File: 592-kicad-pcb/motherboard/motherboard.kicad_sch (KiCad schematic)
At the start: 10 parts, among them U10 NUCLEO144-F746ZG, U7 STM32H563ZITx

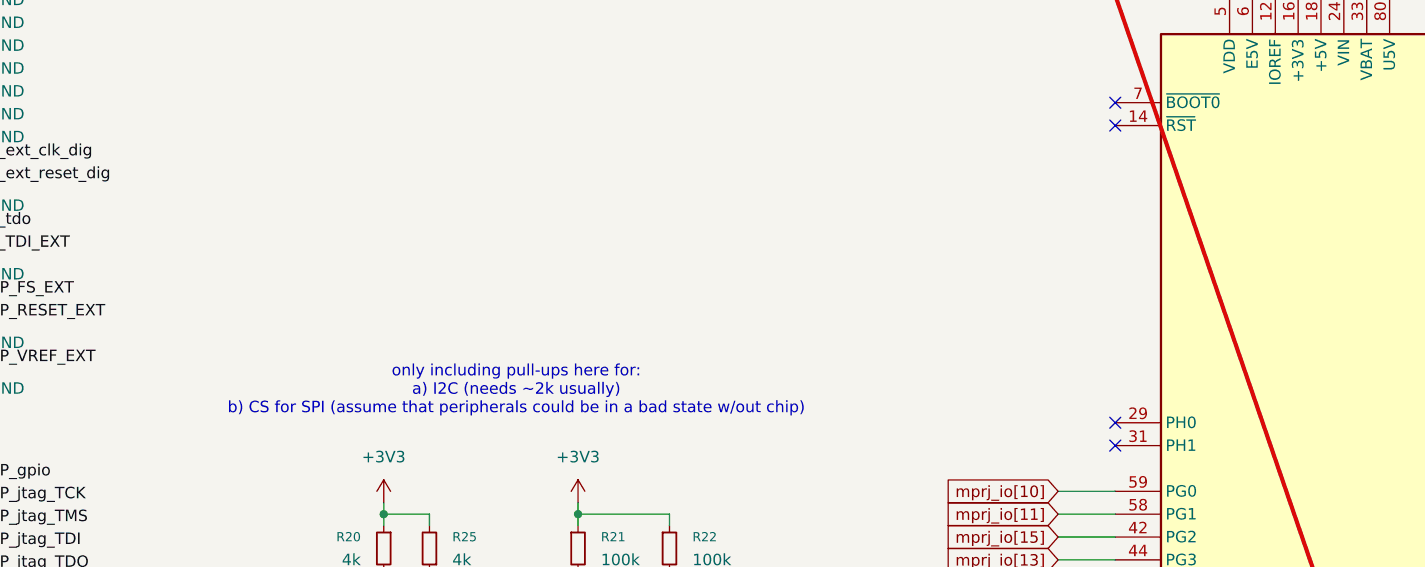
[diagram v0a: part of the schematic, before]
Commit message: add jlc stackup, size pulldowns
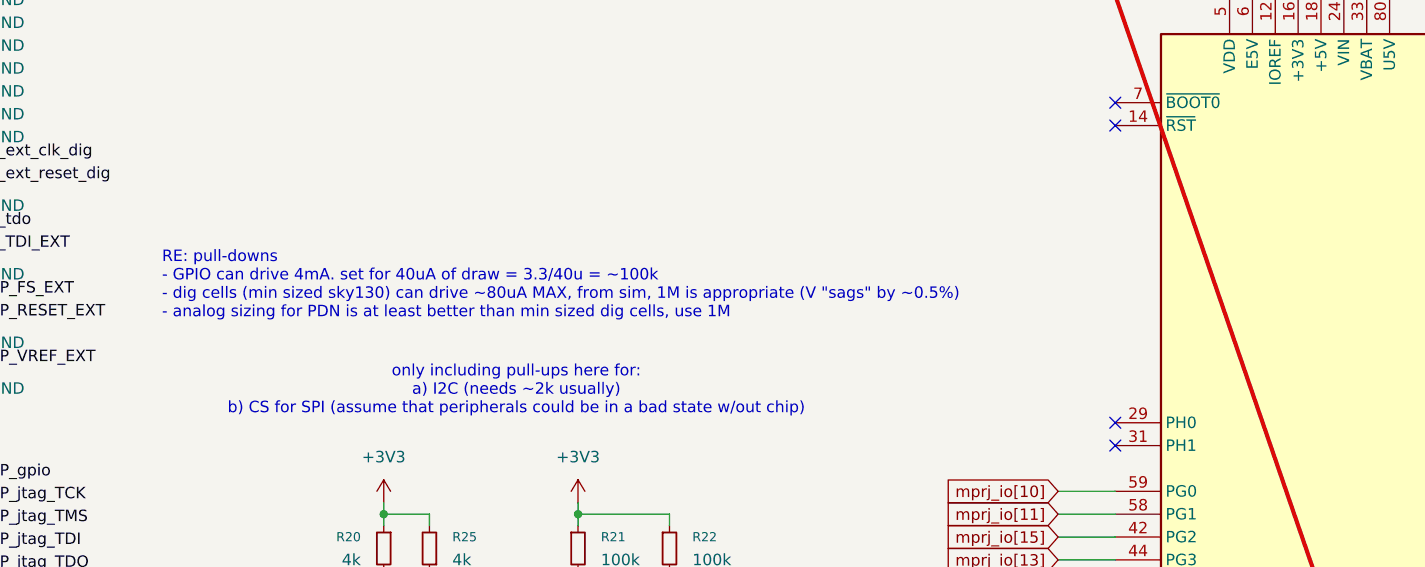
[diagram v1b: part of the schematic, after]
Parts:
- R12, R13, R20, R21, R22, R25: footprint (none) -> Resistor_SMD:R_0603_1608Metric
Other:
- note added: "RE: pull-downs - GPIO can drive 4mA. set for 40uA of draw = 3.3/40u = ~100k - dig cells (min sized sky130) can drive ~80uA MAX, from sim, 1M is appropriate (V "sags" by ~0.5%) - analog sizing for PDN is at least better than min sized dig cells, use 1M"

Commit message: rough layout stufF
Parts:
- U7: footprint Package_QFP:LQFP-144_20x20mm_P0.5mm -> (none)

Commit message: Added most of nucleo domain to the motherboard schematic
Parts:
- added C12: 10uF, symbol Device:C
- added C13: 0.1uF, symbol Device:C
- added C14: 0.01uf - CC0805JRX7R9BB103, Capacitor_SMD:C_0805_2012Metric, symbol Device:C
- added C15, C16, C17, C18, C19, C20, C21, C22, C23, C4: 0.1uf - CC0805KRX7R9BB104, Capacitor_SMD:C_0805_2012Metric, symbol Device:C
- added D1, D2: LED - 17-215SURC/S530-A2/TR8, LED_SMD:LED_1206_3216Metric, symbol Device:LED
- added J10: Conn_01x02_Male, Connector_PinHeader_2.54mm:PinHeader_1x02_P2.54mm_Vertical, symbol Connector:Conn_01x02_Male
- added J11: Conn_01x02_Female, Connector_PinHeader_2.54mm:PinHeader_1x02_P2.54mm_Vertical, symbol Connector:Conn_01x02_Female
- added R30, R37, R38, R39, R40, R41, R42, R43, R44, R45, R46, R47, R48: 10k - RC0805FR-0710KL, Resistor_SMD:R_0805_2012Metric, symbol Device:R
- added R31: 12K 1% - 0805W8F1202T5E, Resistor_SMD:R_0805_2012Metric, symbol Device:R
- added R33, R34: 150 - 0805W8J0151T5E, Resistor_SMD:R_0805_2012Metric, symbol Device:R
- added R35, R36: 10k, Resistor_SMD:R_0805_2012Metric, symbol Device:R
- added U11: SD Card Holder, symbol New_Library:sd_card_connector
- added U12: ~, symbol New_Library:usb_C_Connector
- added U13: FT232H, Package_DFN_QFN:QFN-48-1EP_8x8mm_P0.5mm_EP6.2x6.2mm, symbol Interface_USB:FT232H
- added U14, U15: SN74LVC1G125DCKR, SOT65P210X110-5N, symbol Caravel_board:SN74LVC1G125DCKR
- added U16, U17: W25Q32JVZP, strive_foot_prints:SOIC127P790X216-8N, symbol Caravel_board:W25Q32FVSS
- added X1: DSC6001_10MHZ, strive_foot_prints:DSC6001JE1A-010.0000, symbol Oscillator:XO91
- added Y3: CSTNE12M0GH5L000R0, strive_foot_prints:CSTNE12M0GH5L000R0, symbol Device:Crystal_GND2
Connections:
- net MCU_SDA is gone; now on net I2C1_SDA: R13.1, U10.77 (PB9)
- net +3V3: now also C4.2, X1.4 (V+)
- net CHIP_spi_flash_0_cs_0: now also R37.1, U11.2 (CD/DAT3), U16.1 (~{CS})
- net CHIP_spi_flash_0_dq_0: now also R40.1, U11.3 (CMD), U16.5 (SI(D0))
- net CHIP_spi_flash_0_dq_1: now also R38.1, U11. (CLK), U16.2 (SO(D1))
- net CHIP_spi_flash_0_dq_2: now also R39.1, U16.3 (~{WP}(D2))
- net CHIP_spi_flash_0_dq_3: now also R42.1, U16.7 (~{HOLD}(D3))
- net CHIP_spi_flash_0_sck: now also R41.1, U11. (CLK), U16.6 (SCK)
- net GND: now also C12.2, C13.2, C14.1, C15.1, C16.1, C17.1, C18.1, C19.1, C20.1, C21.1, C22.2, C23.2, C4.1, J10.2 (Pin_2), J11.1 (Pin_1), R31.1, U11. (CLK), U12.A1 (GND), U12.A12 (GND), U12.B1 (GND), U12.B12 (GND), U13.10 (GND), U13.11 (GND), U13.22 (GND), U13.23 (GND), U13.35 (GND), U13.36 (GND), U13.4 (AGND), U13.41 (AGND), U13.42 (TEST), U13.47 (GND), U13.48 (GND), U13.9 (AGND), U14.3 (GND), U15.3 (GND), U16.4 (GND), U17.4 (GND), X1.2 (GND), Y3.2
- net ~{MR}: now also U13.25 (ACBUS1)
- net I2C2_SDA: now reaches U7.10 (PF0)
- net I2C2_SCL: now reaches U7.11 (PF1)
- net SPI1_MISO: now reaches U7.124 (PG9)
- net I2C1_SCL: now reaches U7.136 (PB6)
- net I2C1_SDA: now reaches U7.137 (PB7)
- net I3C1_SCL: now reaches U7.15 (PF5)
- net SPI2_MOSI: now reaches U7.27 (PC1)
- net SPI2_MISO: now reaches U7.28 (PC2)
- net UART4_TX: now reaches U7.34 (PA0)
- net ADC1_INP1: now reaches U7.35 (PA1)
- net SPI1_SCK: now reaches U7.41 (PA5)
- net ADC1_INP3: now reaches U7.42 (PA6)
- net SPI1_MOSI: now reaches U7.43 (PA7)
- net ADC2_INP4: now reaches U7.44 (PC4)
- net ADC2_INP2: now reaches U7.53 (PF13)
- net I3C1_SDA: now reaches U7.55 (PF15)
- net SPI2_SCK: now reaches U7.69 (PB10)
- net UART5_RX: now reaches U7.73 (PB12)
- net UART5_RX: now also U7.74 (PB13)
- net UART4_RX: now reaches U7.80 (PD11)
- new net: U13.1 (XCSI), Y3.1
- new net: U13.2 (XCSO), Y3.3
- new net: D2.1 (K), U13.26 (ACBUS2)
- new net: D1.1 (K), U13.27 (ACBUS3)
- new net: C14.2, R30.1, U13.34 (~{RESET})
- new net: C16.2, U13.37 (VCCA)
- new net: C15.2, U13.38 (VCCCORE)
- new net: R31.2, U13.5 (REF)
- new net: D1.2 (A), R33.1
- new net: J10.1 (Pin_1), X1.1 (EN)
- new net: D2.2 (A), R34.1
- new net +3.3V: C12.1, C13.1, C22.1, C23.1, R35.1, R36.1, R37.2, R38.2, R39.2, R40.2, R41.2, R42.2, R43.2, R44.2, R45.2, R46.2, R47.2, R48.2, U11.4 (VDD), U14.5 (VCC), U15.5 (VCC), U16.8 (VCC), U17.8 (VCC)
- new net EN_V1.8: U13.29 (ACBUS5)
- new net EN_V3.3: U13.30 (ACBUS6)
- new net FTDI_D+: U12.A6 (D+), U12.B6 (D+), U13.7 (DP)
- new net FTDI_D-: U12.A7 (D-), U12.B7 (D-), U13.6 (DM)
- new net FTDI_V3.3: C17.2, C18.2, C19.2, C20.2, C21.2, R30.2, R33.2, R34.2, U13.12 (VCCIO), U13.24 (VCCIO), U13.3 (VPHY), U13.39 (VCCD), U13.40 (VREGIN), U13.46 (VCCIO), U13.8 (VPLL)
- new net MEM_CS: R43.1, U17.1 (~{CS})
- new net MEM_SCK: R47.1, U17.6 (SCK)
- new net MEM_SI: R46.1, U17.5 (SI(D0))
- new net MEM_SO: R44.1, U17.2 (SO(D1))
- new net USB_CS1: U13.16 (ADBUS3)
- new net USB_SCK_TXD: U13.13 (ADBUS0), U14.2 (A)
- new net USB_SI: U13.15 (ADBUS2)
- new net USB_SO_RXD: U13.14 (ADBUS1), U15.4 (Y)
- new net mprj_io[5]_ser_rx: U14.4 (Y)
- new net mprj_io[6]_ser_tx: U15.2 (A)
- new net xclk: X1.3 (OUT)
- new net ~{MEM_HOLD}: R48.1, U17.7 (~{HOLD}(D3))
- new net ~{MEM_WP}: R45.1, U17.3 (~{WP}(D2))
- new net ~{UART_EN}: J11.2 (Pin_2), R35.2, R36.2, U13.21 (ACBUS0), U14.1 (~{OE}), U15.1 (~{OE})
- no-connect marks 39 -> 49
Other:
- note added: "Buffers to enable FTDI UART interface"
- note added: "Caravel 10MHz Clock Source"
- note added: "FTDI Module"
- note added: "Flash memory interface with Caravel"
- note added: "Flash memory interface with Rocket Chip (IF SD CARD WILL NOT WORK)"
- note added: "NOTE: Leave DAT2 and DAT1 unconnected as they are not used in SPI Mode"
- note added: "SD Memory Card Holder (ONLY USE IF FOUND TO BE WORKING)"
- note added: "TODO: Maybe add 10kOhm pull up resistors to CMD, DAT0, and CD/DAT3"
- note added: "TODO: Potentially connect to clock module?"
- note added: "TODO: check the configuration for dq_2 and dq_3 to determine whether the signals need to be inverted"
- note added: "USB_C_Connector_FTDI"
- moved on the sheet: R12, R13, U10

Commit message: resaved maybe more updates on the motherboard schematic
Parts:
- removed C23: 0.1uf - CC0805KRX7R9BB104, Capacitor_SMD:C_0805_2012Metric, symbol Device:C
- removed R43, R44, R45, R46, R47, R48: 10k - RC0805FR-0710KL, Resistor_SMD:R_0805_2012Metric, symbol Device:R
- removed U17: W25Q32JVZP, strive_foot_prints:SOIC127P790X216-8N, symbol Caravel_board:W25Q32FVSS
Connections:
- net SPI1_SCK: now also U7.126 (PG11); no longer U7.41 (PA5)
- net GPIO_Output: now reaches U7.114 (PD0)
- net GPIO_Output: now also U7.115 (PD1), U7.116 (PD2)
- net DAC1_OUT1: now reaches U7.40 (PA4)
- new net DAC1_OUT2: U7.41 (PA5)
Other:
- note added: "Not sure what this does/what it needs to connect to on the Nucleo"
- note added: "TODO: Find out what the hell this connects to"
- note removed: "Flash memory interface with Caravel"
- note removed: "TODO: Potentially connect to clock module?"
- moved on the sheet: U7

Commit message: Added the irq and irq2 inputs to the nucleo
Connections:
- net GPIO_Output is gone; now on net CHIP_i2c_0_scl (irq2 on Caravan): U7.114 (PD0), U7.115 (PD1), U7.116 (PD2)
- net xclk is gone; now on net CHIP_clk: X1.3 (OUT)
- net MCU_TIM_NFCCLK: now also U7.60 (PE9)
- net CHIP_i2c_0_scl (irq2 on Caravan): now reaches U7.117 (PD3)
- net CHIP_i2c_0_scl (irq2 on Caravan): now also U7.118 (PD4)
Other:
- note removed: "Not sure what this does/what it needs to connect to on the Nucleo"
- note removed: "TODO: Find out what the hell this connects to"

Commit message: Added the rest of the ports
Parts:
- C15, C16, C17, C18, C19, C20, C21, C22, C4: value 0.1uf - CC0805KRX7R9BB104 -> 0.1uf
- R33, R34: value 150 - 0805W8J0151T5E -> 150
- R37, R38, R39, R40, R41, R42: value 10k - RC0805FR-0710KL -> 10k
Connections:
- net ~{MR}: no longer U13.25 (ACBUS1)
- net EN_V1.8: no longer names the net of U13.29 (ACBUS5)
- net EN_V3.3: no longer names the net of U13.30 (ACBUS6)
- net FTDI_V3.3 renamed 3V3
- net mprj_io[5]_ser_rx renamed CHIP_spi_0_dq_0 (ser_rx on Caravan)
- net mprj_io[6]_ser_tx renamed CHIP_spi_0_cs_0 (ser_tx on Caravan)

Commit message: clean up schematics, add proper connectors
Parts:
- removed C12: 10uF, symbol Device:C
- removed C13: 0.1uF, symbol Device:C
- removed C14: 0.01uf - CC0805JRX7R9BB103, Capacitor_SMD:C_0805_2012Metric, symbol Device:C
- removed C15, C16, C17, C18, C19, C20, C21, C22, C4: 0.1uf, Capacitor_SMD:C_0805_2012Metric, symbol Device:C
- removed CON1, CON2: ~, TinyTapeout:FH-00148_PinSocket_2x20_P2.54mm, symbol Connector_Generic:Conn_02x20_Odd_Even
- removed D1, D2: LED - 17-215SURC/S530-A2/TR8, LED_SMD:LED_1206_3216Metric, symbol Device:LED
- removed J10: Conn_01x02_Male, Connector_PinHeader_2.54mm:PinHeader_1x02_P2.54mm_Vertical, symbol Connector:Conn_01x02_Male
- removed J11: Conn_01x02_Female, Connector_PinHeader_2.54mm:PinHeader_1x02_P2.54mm_Vertical, symbol Connector:Conn_01x02_Female
- removed R12, R13, R20, R25: 4k, Resistor_SMD:R_0603_1608Metric, symbol Device:R_Small
- removed R21, R22: 100k, Resistor_SMD:R_0603_1608Metric, symbol Device:R_Small
- removed R30: 10k - RC0805FR-0710KL, Resistor_SMD:R_0805_2012Metric, symbol Device:R
- removed R31: 12K 1% - 0805W8F1202T5E, Resistor_SMD:R_0805_2012Metric, symbol Device:R
- removed R33, R34: 150, Resistor_SMD:R_0805_2012Metric, symbol Device:R
- removed R35, R36, R37, R38, R39, R40, R41, R42: 10k, Resistor_SMD:R_0805_2012Metric, symbol Device:R
- removed U10: NUCLEO144-F746ZG, Module:ST_Morpho_Connector_144_STLink, symbol MCU_Module:NUCLEO144-F746ZG
- removed U11: SD Card Holder, symbol New_Library:sd_card_connector
- removed U12: ~, symbol New_Library:usb_C_Connector
- removed U13: FT232H, Package_DFN_QFN:QFN-48-1EP_8x8mm_P0.5mm_EP6.2x6.2mm, symbol Interface_USB:FT232H
- removed U14, U15: SN74LVC1G125DCKR, SOT65P210X110-5N, symbol Caravel_board:SN74LVC1G125DCKR
- removed U16: W25Q32JVZP, strive_foot_prints:SOIC127P790X216-8N, symbol Caravel_board:W25Q32FVSS
- removed X1: DSC6001_10MHZ, strive_foot_prints:DSC6001JE1A-010.0000, symbol Oscillator:XO91
- removed Y3: CSTNE12M0GH5L000R0, strive_foot_prints:CSTNE12M0GH5L000R0, symbol Device:Crystal_GND2
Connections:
- removed net CHIP_i2c_0_scl (irq2 on Caravan): U7.114 (PD0), U7.115 (PD1), U7.116 (PD2), U7.117 (PD3), U7.118 (PD4)
- net DAC1_OUT1 renamed MCU_DAC_VREF
- net I2C1_SCL renamed MCU_SCK
- net I2C1_SDA renamed MCU_SDA
- new net CHIP_i2c_0_scl_(irq2_on_Caravan): U7.118 (PD4)
- new net CHIP_spi_0_sck_(irq_on_Caravan): U7.117 (PD3)
- new net MCU_GPIO_FS_SEL: U7.116 (PD2)
- new net MCU_GPIO_NFCCLK_SEL: U7.115 (PD1)
- new net MCU_GPIO_RESET_AFE: U7.114 (PD0)
- no-connect marks 49 -> 0
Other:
- added sheet chip_connection (chip_connection.kicad_sch)
- added sheet ftdi (ftdi.kicad_sch)
- added sheet memory (memory.kicad_sch)
- sheet clock_sources ports: added CARAVEL_CLK_10M, CARAVEL_CLK_SEL; removed none
- note added: "DAC1_OUT1"
- note added: "GPIO_Output (all on this bank)"
- note added: "I2C1_SCL"
- note added: "I2C1_SDA"
- note added: "MASTER TODO: 1) verify caravel support chip configuration 2) correct pull up/down resistors 3) update to new FTDI chip 4) add voltage regulators 5) update nucleo symbol, assign/document pins 6) verify memory interface pinsouts for rocketchip, add connector 7) make connector pinouts match PMOD/JTAG interface on arty"
- note added: "TIM1_CH1"
- note removed: "Buffers to enable FTDI UART interface"
- note removed: "Caravel 10MHz Clock Source"
- note removed: "FTDI Module"
- note removed: "Flash memory interface with Rocket Chip (IF SD CARD WILL NOT WORK)"
- note removed: "NOTE: Leave DAT2 and DAT1 unconnected as they are not used in SPI Mode"
- note removed: "RE: pull-downs - GPIO can drive 4mA. set for 40uA of draw = 3.3/40u = ~100k - dig cells (min sized sky130) can drive ~80uA MAX, from sim, 1M is appropriate (V "sags" by ~0.5%) - analog sizing for PDN is at least better than min sized dig cells, use 1M"
- note removed: "SD Memory Card Holder (ONLY USE IF FOUND TO BE WORKING)"
- note removed: "TODO: Maybe add 10kOhm pull up resistors to CMD, DAT0, and CD/DAT3"
- note removed: "TODO: check the configuration for dq_2 and dq_3 to determine whether the signals need to be inverted"
- note removed: "TODO: use new zio connector pinout?"
- note removed: "USB_C_Connector_FTDI"
- note removed: "add pull-downs where applicable for inputs to chips from the NFC chip consider just using GPIO PDN on STM. need to add discretes for other chips"
- note removed: "connectors for daughterboard (TODO keep up to date when finalized)"
- note removed: "only including pull-ups here for: a) I2C (needs ~2k usually) b) CS for SPI (assume that peripherals could be in a bad state w/out chip)"
- moved on the sheet: U7

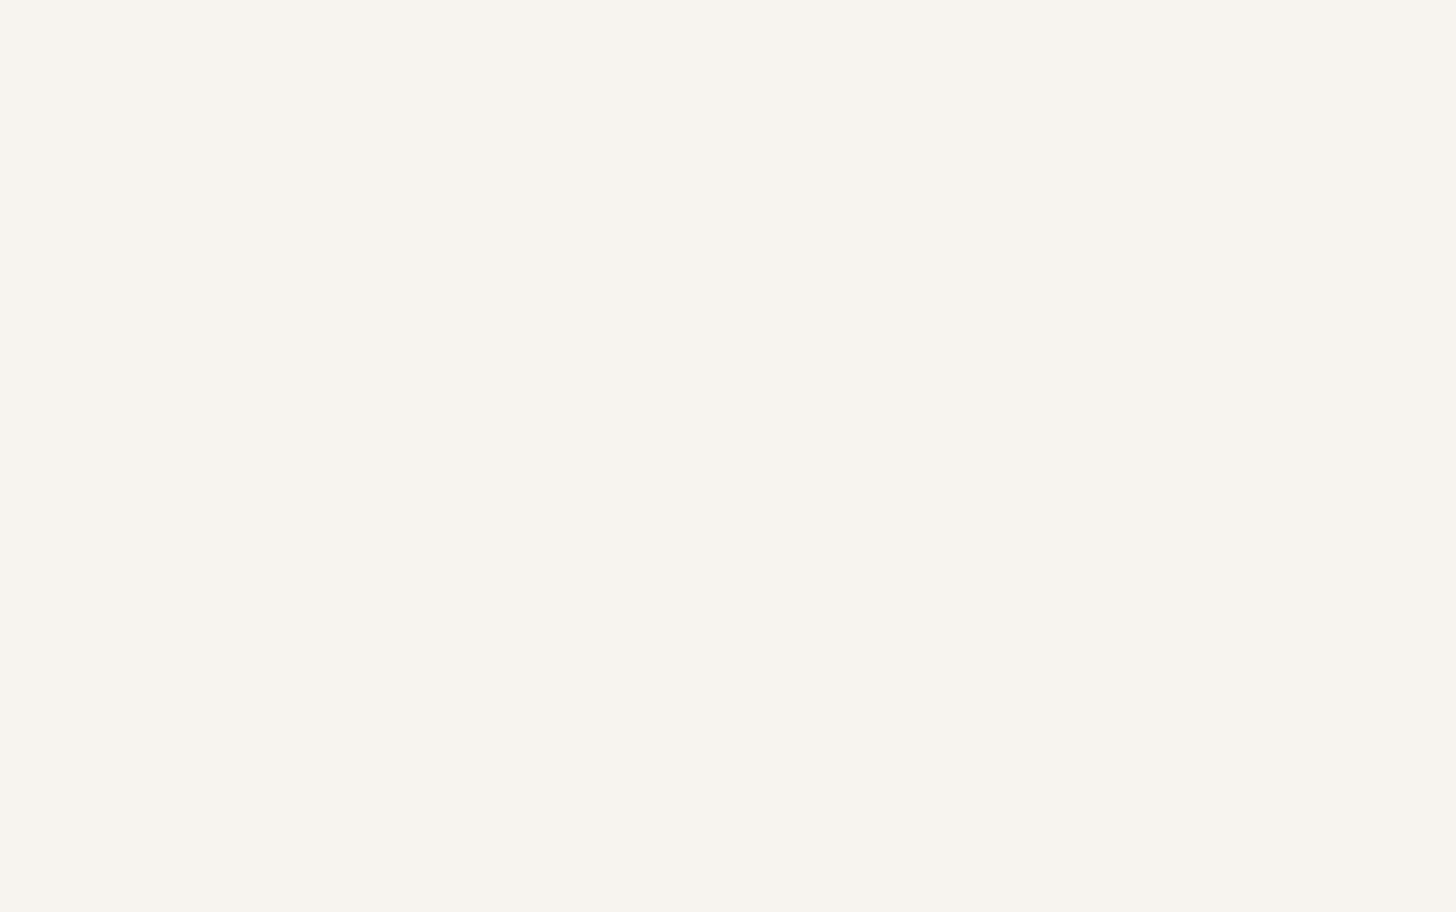
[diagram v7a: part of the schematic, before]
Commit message: update ftdi chip
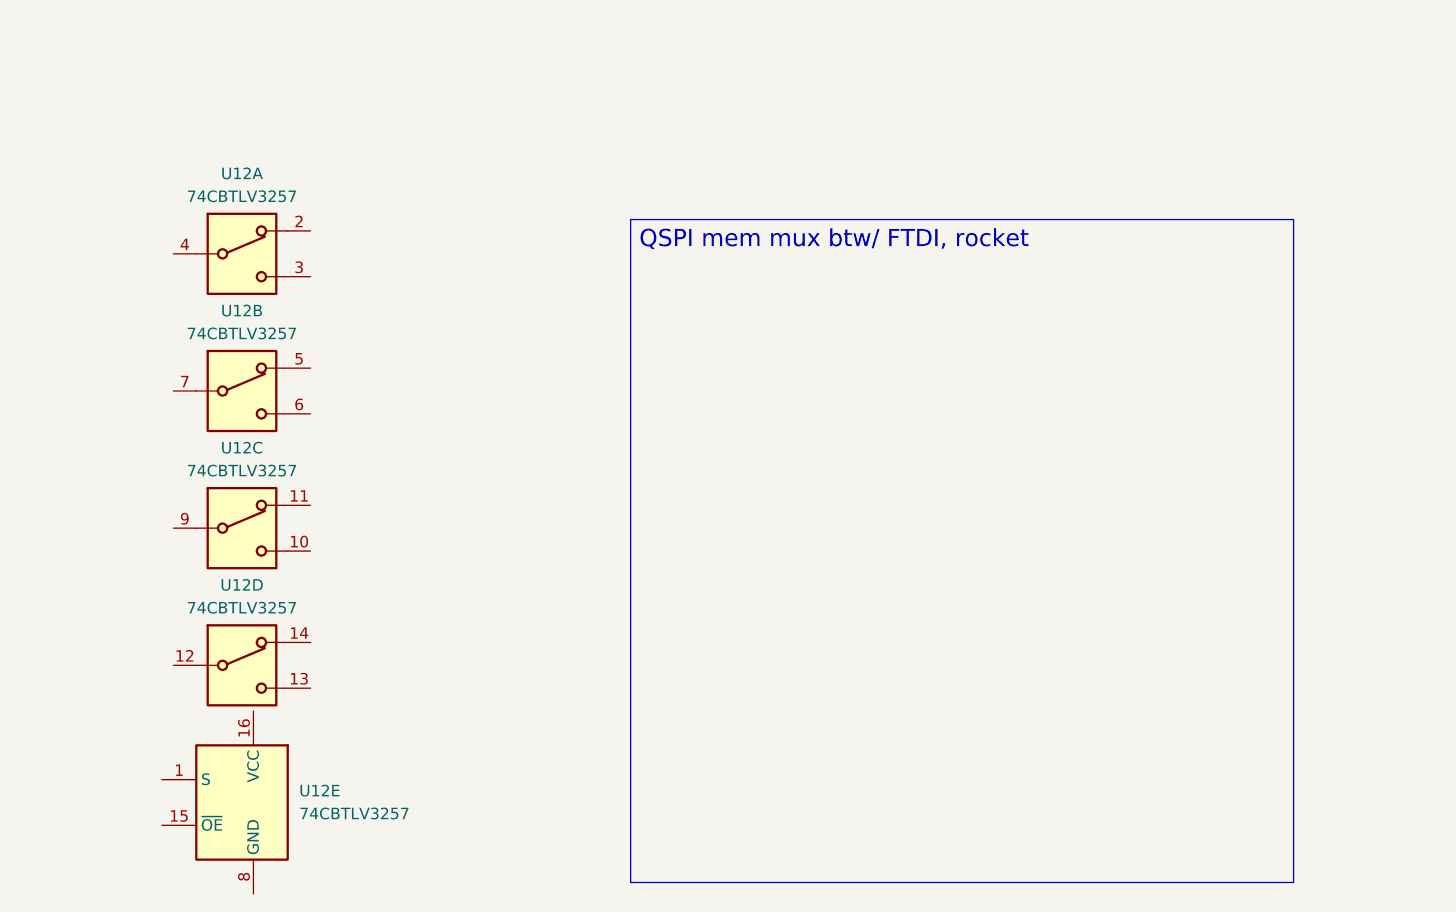
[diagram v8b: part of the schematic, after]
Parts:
- added U12: 74CBTLV3257, symbol 74xx:74CBTLV3257
